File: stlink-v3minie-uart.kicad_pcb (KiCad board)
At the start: 2 copper layers, 14 x 23 mm, 3 parts, among them J1 Conn_01x05, J2 Conn_02x05_Top_Bottom, J3 Conn_01x04_Pin

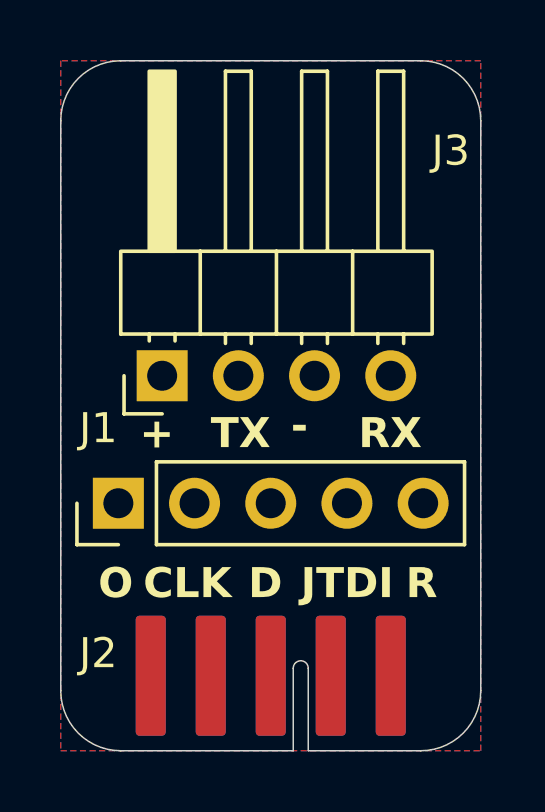
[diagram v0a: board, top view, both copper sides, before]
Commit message: pcb: route and add stitching vias
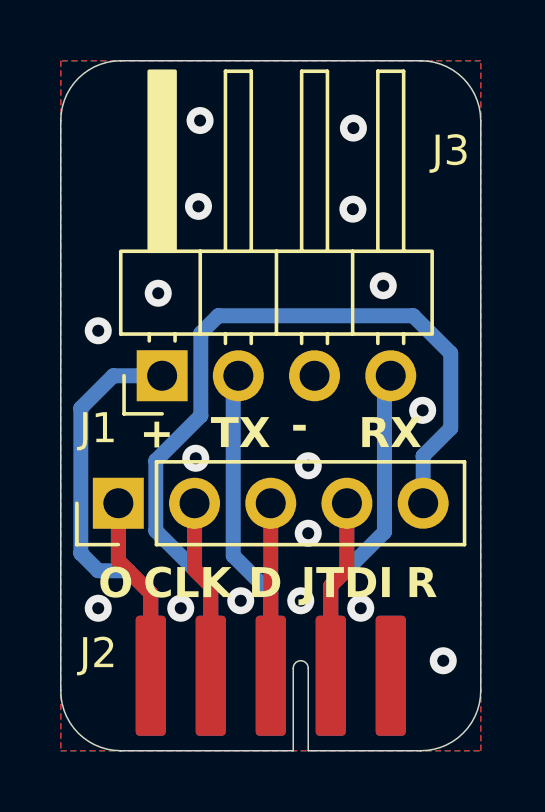
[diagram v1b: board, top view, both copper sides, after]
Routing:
- net /nRST: track 0.00 -> 27.3 mm
- net +3V3: track 0.00 -> 13.6 mm
- net /VCP_RX: track 0.00 -> 10.8 mm
- net /VCP_TX: track 0.00 -> 10.6 mm
- net /SWO: track 0.00 -> 6.20 mm
- net /SWCLK: track 0.00 -> 5.97 mm
- net /JTDI: track 0.00 -> 5.97 mm
- net /SWDIO: track 0.00 -> 5.75 mm
- net GND: vias 0 -> 17

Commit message: pcb(silk): add usr txt
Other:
- board text added: "R01"
- board text added: "Rémi A. 26-06"
- board text added: "ST to UART"
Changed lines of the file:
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@@
+		)
+	)
+	(gr_text "Rémi A. 26-06"
+		(at 156.141734 98.916522 0)
+		(layer "B.SilkS")
+		(effects
+			(font
+				(size 0.9 0.8)
+				(thickness 0.1)
+			)
+			(justify left bottom mirror)
+		)
+	)
+	(gr_text "R01"
+		(at 146.361734 98.916522 0)
+		(layer "B.SilkS")
+		(effects
+			(font
+				(size 0.9 0.9)
+				(thickness 0.1)
+			)
+			(justify left bottom mirror)
+		)
+	)
+	(gr_text "ST to UART"
+		(at 156.361734 96.916522 0)
+		(layer "B.SilkS")
+		(effects
+			(font
+				(size 1.5 1.5)
+				(thickness 0.1875)
+			)
+			(justify left bottom mirror)
 		)
 	)
